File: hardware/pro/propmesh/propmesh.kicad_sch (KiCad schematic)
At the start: 0 parts

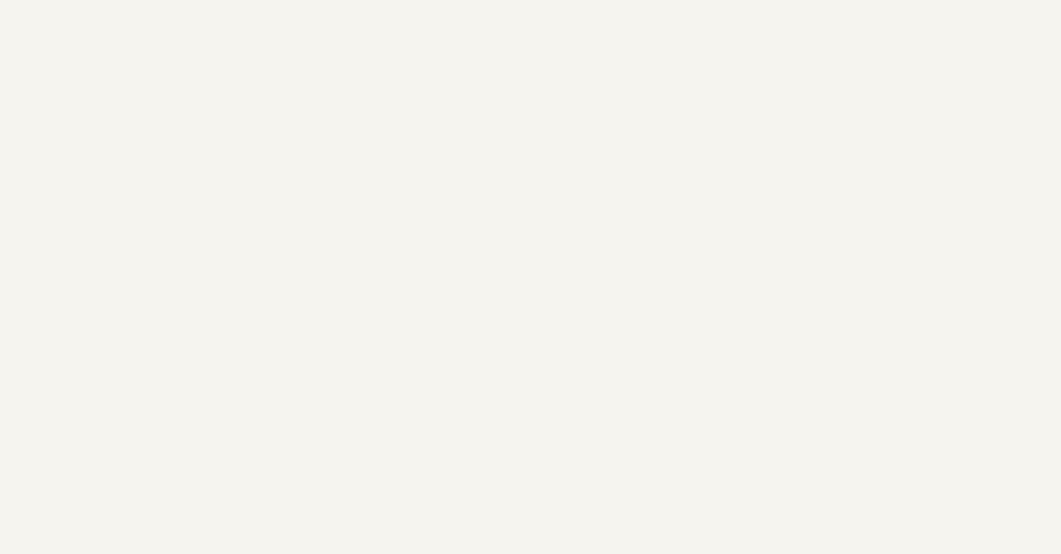
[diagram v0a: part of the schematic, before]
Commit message: Sheet 02 (MCU+USB) captured + GPIO 33/34 pinmap fix + multi-sheet checker
- FINDING: GPIO 33/34 are not bonded out on ANY ESP32-S3-WROOM-1
  variant (Espressif DS v1.8 pin table) — the old open item's premise
  was wrong. MOTOR_B_IN1/IN2 moved to GPIO 35/36, headers regenerated;
  IO37 is now the only spare pin. N8R2 variant is load-bearing twice
  (octal PSRAM consumes IO35-37). Closes verification item #1.
- Sheet 02 drawn and verified: checknet all nets+footprints green,
  ERC clean. Module C3013944, USB-C C165948 (KiCad ships the
  vendor-exact HRO footprint), ST USBLC6, SS34, all sourced with
  verified LCSC numbers; MCU block $4.11@100 vs $3.72 estimate.
- checknet.py grows up for multi-sheet reality: named-net subset
  semantics (rails/global labels span sheets), pairing scoped to the
  spec's home KiCad sheet, orientation-free two-terminal parts,
  multi-pad pins (USB-C 4x VBUS), pad-number-exact pinfunction
  normalization (the SHIELD_SH lesson).
- Cross-sheet GPIO travels by GLOBAL label, spelling machine-checked
  against pinmap.yaml.

Co-Authored-By: Claude Fable 5 <noreply@anthropic.com>
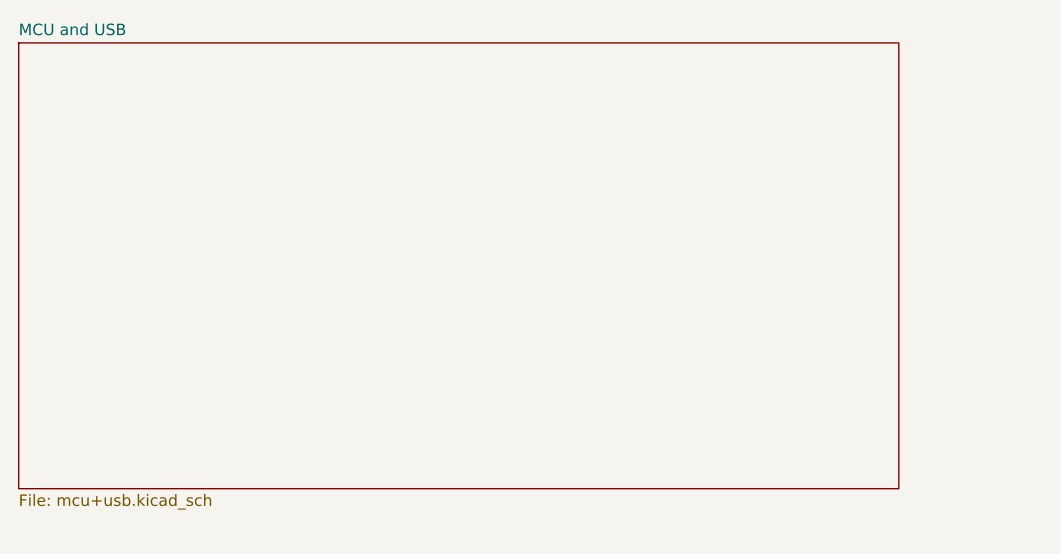
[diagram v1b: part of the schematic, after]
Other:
- added sheet MCU and USB (mcu+usb.kicad_sch)
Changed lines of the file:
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@@
+	)
+	(sheet
+		(at 24.13 22.86)
+		(size 97.79 49.53)
+		(exclude_from_sim no)
+		(in_bom yes)
+		(on_board yes)
+		(dnp no)
+		(fields_autoplaced yes)
+		(stroke
+			(width 0.1524)
+			(type solid)
+		)
+		(fill
+			(color 0 0 0 0)
+		)
+		(property "Sheetname" "MCU and USB"
+			(at 24.13 22.1484 0)
+			(show_name no)
+			(do_not_autoplace no)
+			(effects
+				(font
+					(size 1.27 1.27)
+				)
+				(justify left bottom)
+			)
+		)
+		(property "Sheetfile" "mcu+usb.kicad_sch"
+			(at 24.13 72.9746 0)
+			(show_name no)
+			(do_not_autoplace no)
+			(effects
+				(font
+					(size 1.27 1.27)
+				)
+				(justify left top)
+			)
+		)
+		(instances
+			(project "propmesh"
+				(path "/6aa579d1-bfe0-499b-882d-72f52ff6d36c"
+					(page "3")
+				)
+			)
+		)
 	)
 	(sheet

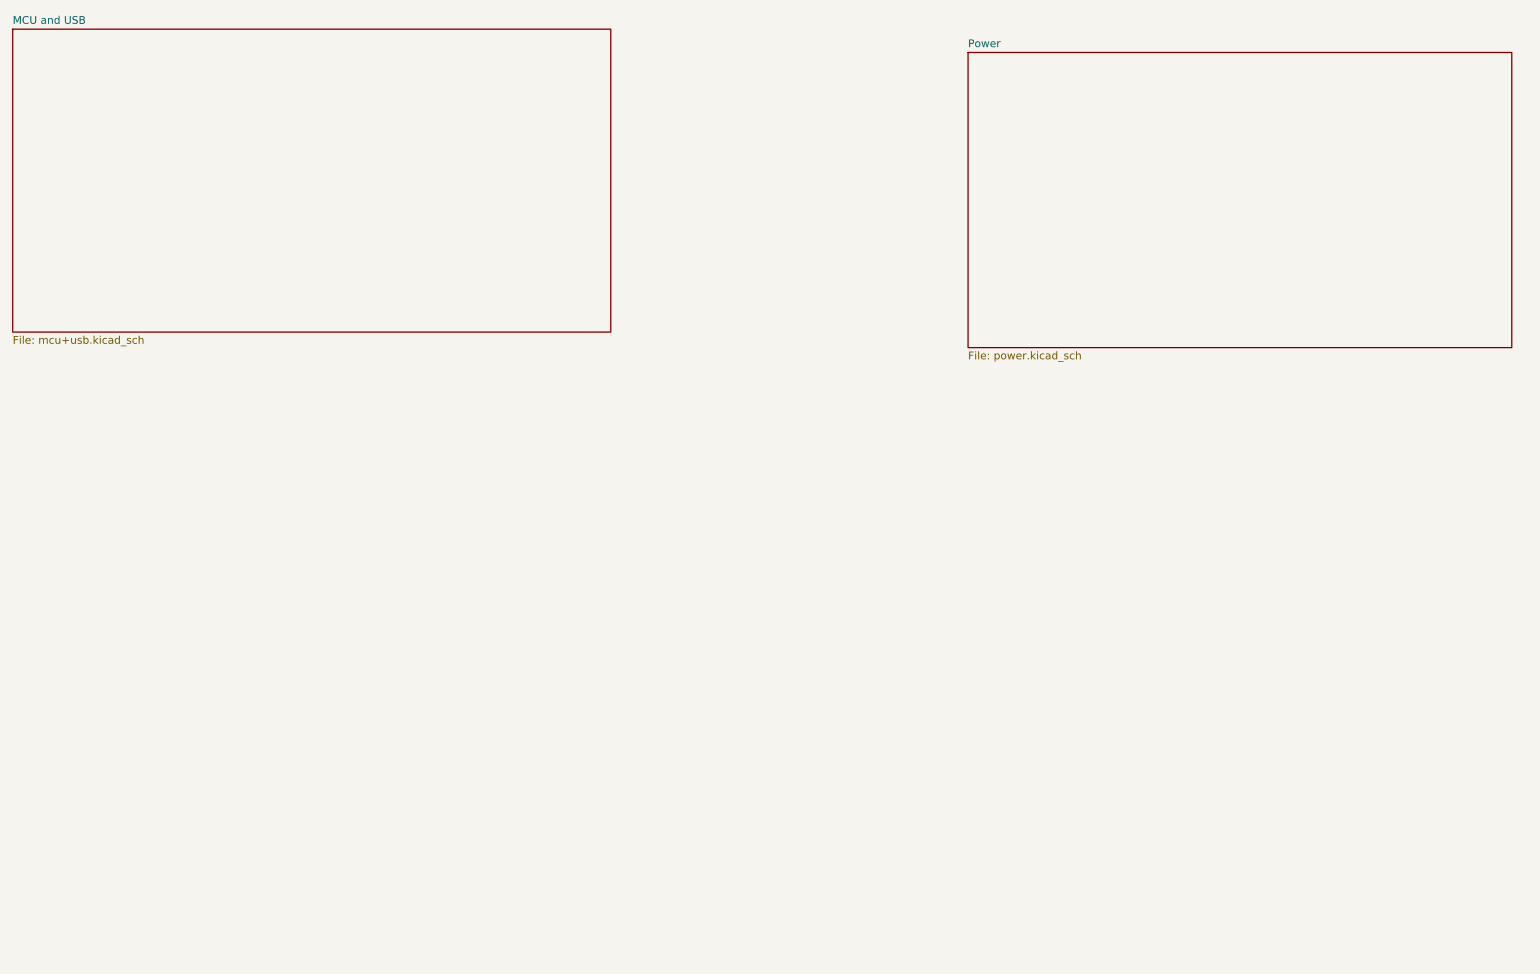
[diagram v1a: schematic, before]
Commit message: Sheet 03 (slow outputs) captured + channel redesign to supply voltage
- LED-channel decision resolved: all 6 channels kept, discrete AO3400A
  low-side FETs (Basic, replaces sheet 06's 2N7002 too — one MOSFET
  part number board-wide); ULN2003 drives relays only
- Channels re-pointed +5V -> VIN_PROT with SS34 flyback per channel:
  2 A/ch, 5 A aggregate, 12/24 V lights and pneumatic solenoids are
  first-class loads. Supply-voltage coupling documented in the spec's
  user guidance (match supply to lights; mixed-voltage recipe)
- HK4100F relay: symbol+footprint imported, land pattern verified,
  EasyEDA inverted-pin defect fixed in library (4th known import lie,
  added to checklist); coil is 40 mA not 70; NO/NC continuity check
  deferred to bring-up by design
- checknet renderer: undrawn power rails annotate inside part boxes
  (no more +5V hairball); roll-call generalised
- All three drawn sheets: checknet green, ERC clean (31 one-sided
  labels pending sheets 04-07). Caught U3's footprint reverted to
  WROOM-1 by Update-from-Library field reset — reassigned, dialog
  gotcha documented

Co-Authored-By: Claude Fable 5 <noreply@anthropic.com>
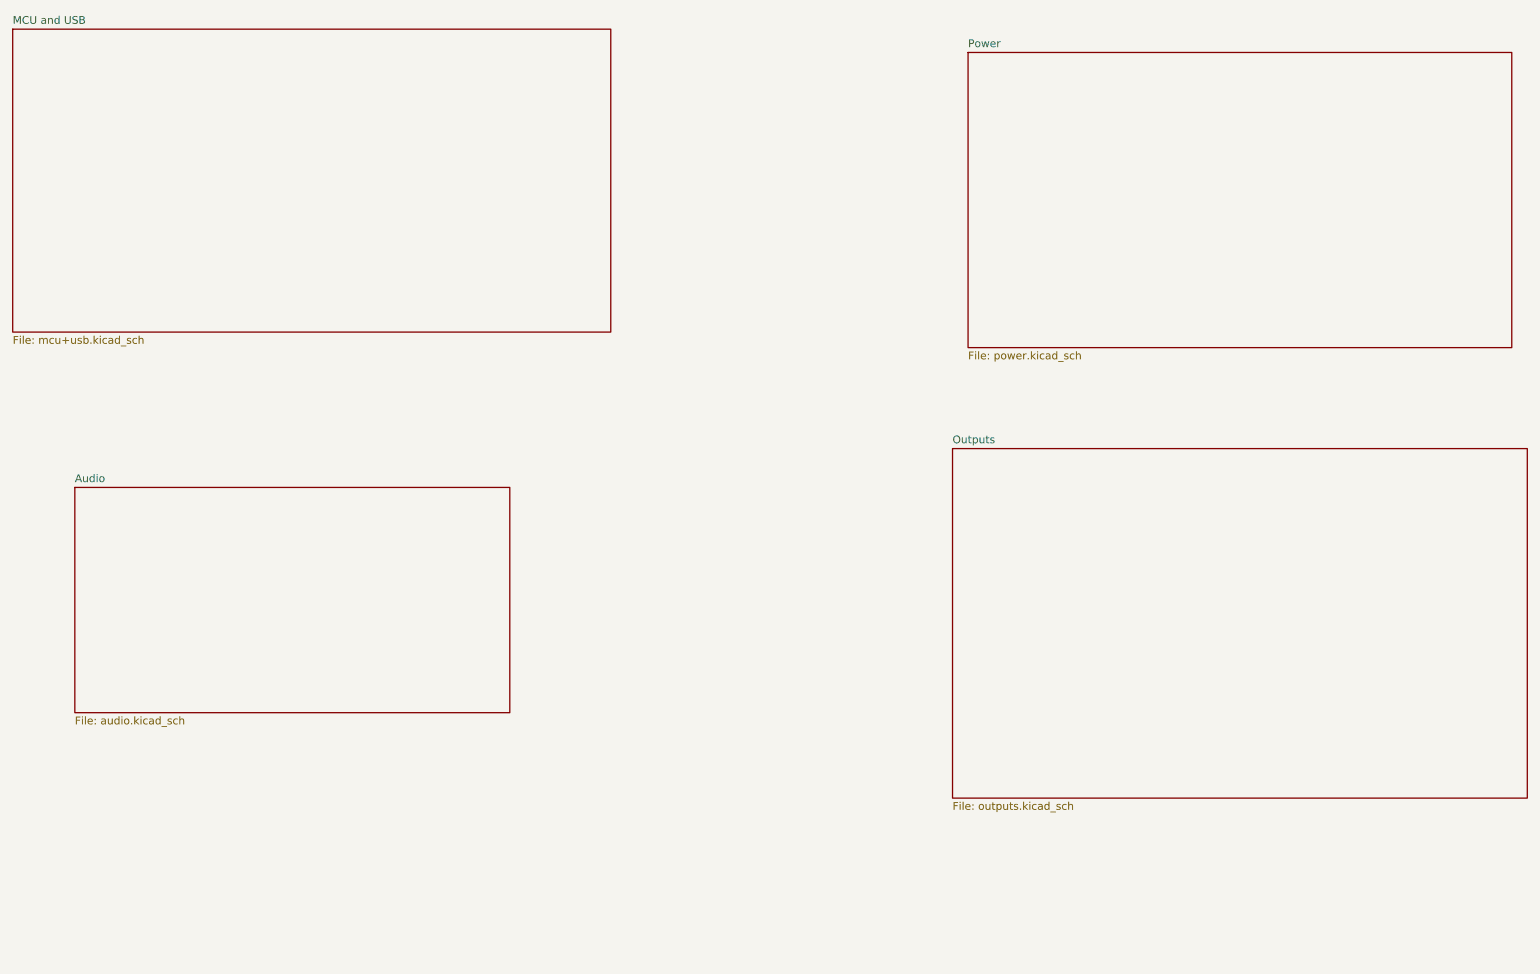
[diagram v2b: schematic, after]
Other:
- added sheet Audio (audio.kicad_sch)
- added sheet Outputs (outputs.kicad_sch)
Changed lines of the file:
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@@
+	)
+	(sheet
+		(at 177.8 91.44)
+		(size 93.98 57.15)
+		(exclude_from_sim no)
+		(in_bom yes)
+		(on_board yes)
+		(dnp no)
+		(fields_autoplaced yes)
+		(stroke
+			(width 0.1524)
+			(type solid)
+		)
+		(fill
+			(color 0 0 0 0)
+		)
+		(property "Sheetname" "Outputs"
+			(at 177.8 90.7284 0)
+			(show_name no)
+			(do_not_autoplace no)
+			(effects
+				(font
+					(size 1.27 1.27)
+				)
+				(justify left bottom)
+			)
+		)
+		(property "Sheetfile" "outputs.kicad_sch"
+			(at 177.8 149.1746 0)
+			(show_name no)
+			(do_not_autoplace no)
+			(effects
+				(font
+					(size 1.27 1.27)
+				)
+				(justify left top)
+			)
+		)
+		(instances
+			(project "propmesh"
+				(path "/6aa579d1-bfe0-499b-882d-72f52ff6d36c"
+					(page "4")
+				)
+			)
+		)
 	)
 	(sheet
@@
 				)
 			)
+		)
+	)
+	(sheet
+		(at 34.29 97.79)
+		(size 71.12 36.83)
+		(exclude_from_sim no)
+		(in_bom yes)
+		(on_board yes)
+		(dnp no)
+		(fields_autoplaced yes)
+		(stroke
+			(width 0.1524)
+			(type solid)
+		)
+		(fill
+			(color 0 0 0 0)
+		)
+		(property "Sheetname" "Audio"
+			(at 34.29 97.0784 0)
+			(show_name no)
+			(do_not_autoplace no)
+			(effects
+				(font
+					(size 1.27 1.27)
+				)
+				(justify left bottom)
+			)
+		)
+		(property "Sheetfile" "audio.kicad_sch"
+			(at 34.29 135.2046 0)
+			(show_name no)
+			(do_not_autoplace no)
+			(effects
+				(font
+					(size 1.27 1.27)
+				)
+				(justify left top)
+			)
+		)
+		(instances
+			(project "propmesh"
+				(path "/6aa579d1-bfe0-499b-882d-72f52ff6d36c"
+					(page "5")
+				)
+			)

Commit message: Sheet 06 (motors) captured: stepper sockets + DRV8871, all spec unknowns closed
- Open item #3 CLOSED from the Pololu md09b drawing: StepStick rows
  12.70 mm apart exactly, 1x8 @ 2.54; RST/SLP positions hardwired
  together = A4988-legal AND the TMC2209 PDN_UART bus (shared, both
  sockets, MS1/MS2 straps = addresses); DIAG via per-socket aux
  headers + bridged solder jumpers (vendor positions differ);
  1k series on GPIO43 (U0TXD boot log)
- ILIM verified from TI DS: ITRIP = 64000/R; 30k = 2.13 A/channel
- Import lie #6 caught: DRV8871's generic footprint name collided
  with the AP64350's and --overwrite silently replaced it (geometry
  happened to be identical; only the LCSC property flipped). Restored
  + forked to SO-8EP_DRV8871DDAR; post-import git-status rule added
- checknet: name-aware tie-breaks — six identical strap headers on
  six identically-shaped nets defeated value-level pairing and
  reported phantom crosses on a perfectly-wired sheet; user labels
  now arbitrate ties. All five drawn sheets re-verified green
- DRV8871 pin types set in library; ERC clean board-wide
- Motor block $4.75@100 verified (DRV8871 genuine = 2x the old
  estimate); duty-paid ~$49.52. CLAUDE.md verification item #3 closed
  (last hardware unknown in the spec)

Co-Authored-By: Claude Fable 5 <noreply@anthropic.com>
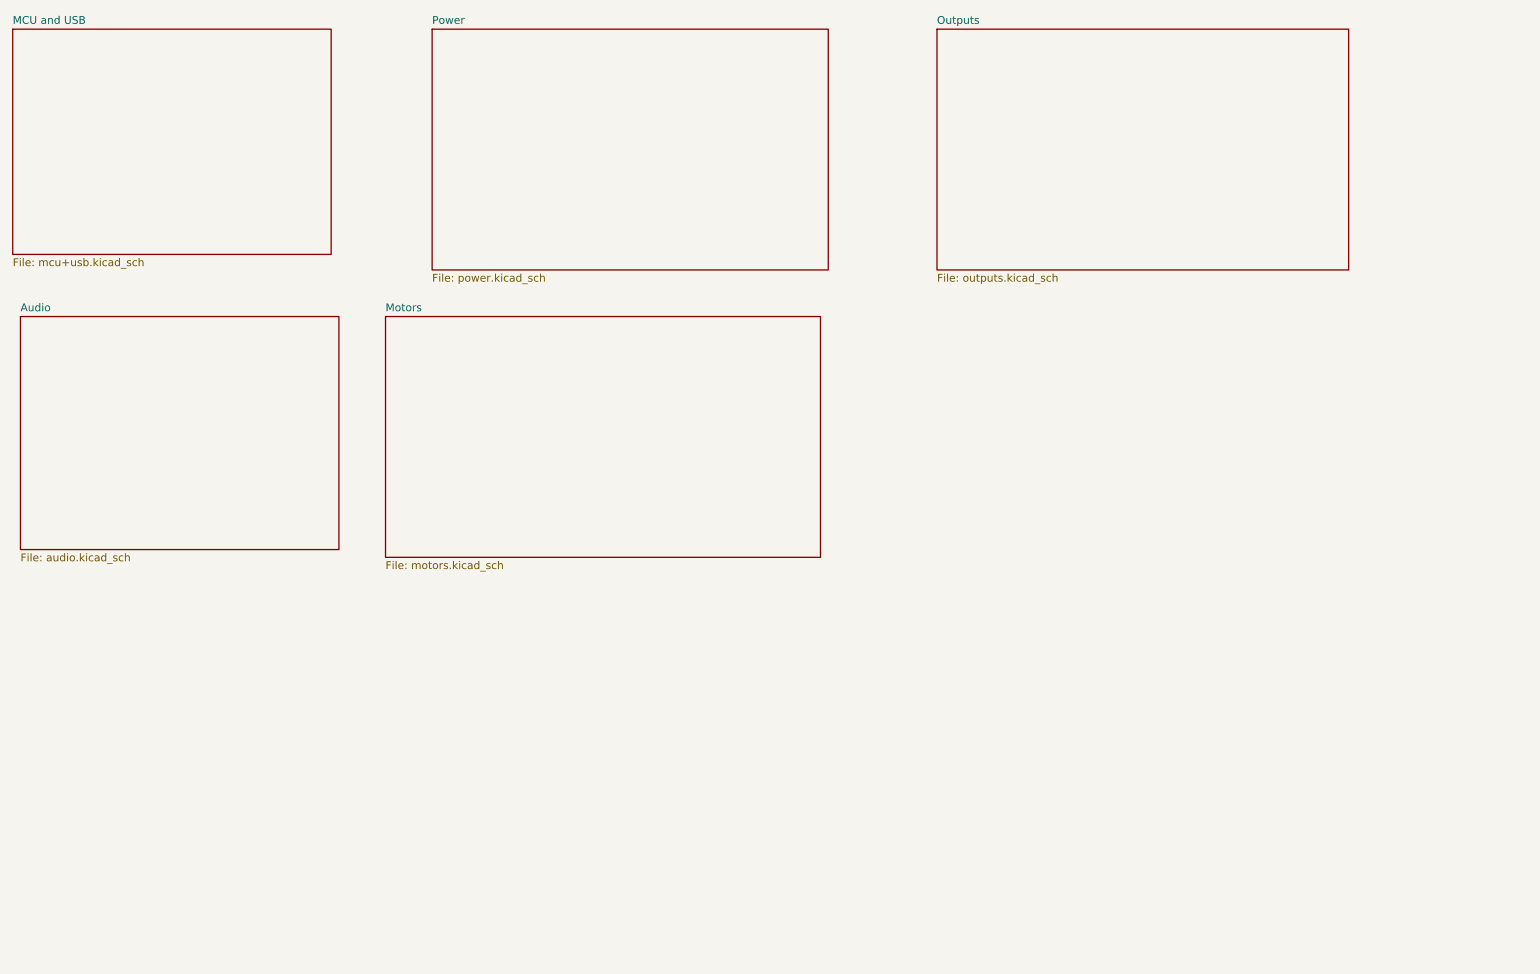
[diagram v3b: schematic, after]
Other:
- added sheet Motors (motors.kicad_sch)
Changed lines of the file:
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@@
 	(sheet
 		(at 24.13 22.86)
-		(size 97.79 49.53)
+		(size 52.07 36.83)
 		(exclude_from_sim no)
 		(in_bom yes)
@@
 		)
 		(property "Sheetfile" "mcu+usb.kicad_sch"
-			(at 24.13 72.9746 0)
+			(at 24.13 60.2746 0)
 			(show_name no)
 			(do_not_autoplace no)
@@
 	)
 	(sheet
-		(at 177.8 91.44)
-		(size 93.98 57.15)
+		(at 175.26 22.86)
+		(size 67.31 39.37)
 		(exclude_from_sim no)
 		(in_bom yes)
@@
 		)
 		(property "Sheetname" "Outputs"
-			(at 177.8 90.7284 0)
+			(at 175.26 22.1484 0)
 			(show_name no)
 			(do_not_autoplace no)
@@
 		)
 		(property "Sheetfile" "outputs.kicad_sch"
-			(at 177.8 149.1746 0)
+			(at 175.26 62.8146 0)
 			(show_name no)
 			(do_not_autoplace no)
@@
 	)
 	(sheet
-		(at 180.34 26.67)
-		(size 88.9 48.26)
+		(at 92.71 22.86)
+		(size 64.77 39.37)
 		(exclude_from_sim no)
 		(in_bom yes)
@@
 		)
 		(property "Sheetname" "Power"
-			(at 180.34 25.9584 0)
+			(at 92.71 22.1484 0)
 			(show_name yes)
 			(do_not_autoplace no)
@@
 		)
 		(property "Sheetfile" "power.kicad_sch"
-			(at 180.34 75.5146 0)
+			(at 92.71 62.8146 0)
 			(show_name no)
 			(do_not_autoplace no)
@@
 	)
 	(sheet
-		(at 34.29 97.79)
-		(size 71.12 36.83)
+		(at 85.09 69.85)
+		(size 71.12 39.37)
+		(exclude_from_sim no)
+		(in_bom yes)
+		(on_board yes)
+		(dnp no)
+		(fields_autoplaced yes)
+		(stroke
+			(width 0.1524)
+			(type solid)
+		)
+		(fill
+			(color 0 0 0 0)
+		)
+		(property "Sheetname" "Motors"
+			(at 85.09 69.1384 0)
+			(show_name no)
+			(do_not_autoplace no)
+			(effects
+				(font
+					(size 1.27 1.27)
+				)
+				(justify left bottom)
+			)
+		)
+		(property "Sheetfile" "motors.kicad_sch"
+			(at 85.09 109.8046 0)
+			(show_name no)
+			(do_not_autoplace no)
+			(effects
+				(font
+					(size 1.27 1.27)
+				)
+				(justify left top)
+			)
+		)
+		(instances
+			(project "propmesh"
+				(path "/6aa579d1-bfe0-499b-882d-72f52ff6d36c"
+					(page "6")
+				)
+			)
+		)
+	)
+	(sheet
+		(at 25.4 69.85)
+		(size 52.07 38.1)
 		(exclude_from_sim no)
 		(in_bom yes)
@@
 		)
 		(property "Sheetname" "Audio"
-			(at 34.29 97.0784 0)
+			(at 25.4 69.1384 0)
 			(show_name no)
 			(do_not_autoplace no)
@@
 		)
 		(property "Sheetfile" "audio.kicad_sch"
-			(at 34.29 135.2046 0)
-			(show_name no)
-			(do_not_autoplace no)
+			(at 25.4 108.5346 0)
+			(show_name no)
+			(do_not_autoplace no)
